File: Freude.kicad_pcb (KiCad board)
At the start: 4 copper layers, 1 part, among them U1 1CA027Pinnacle

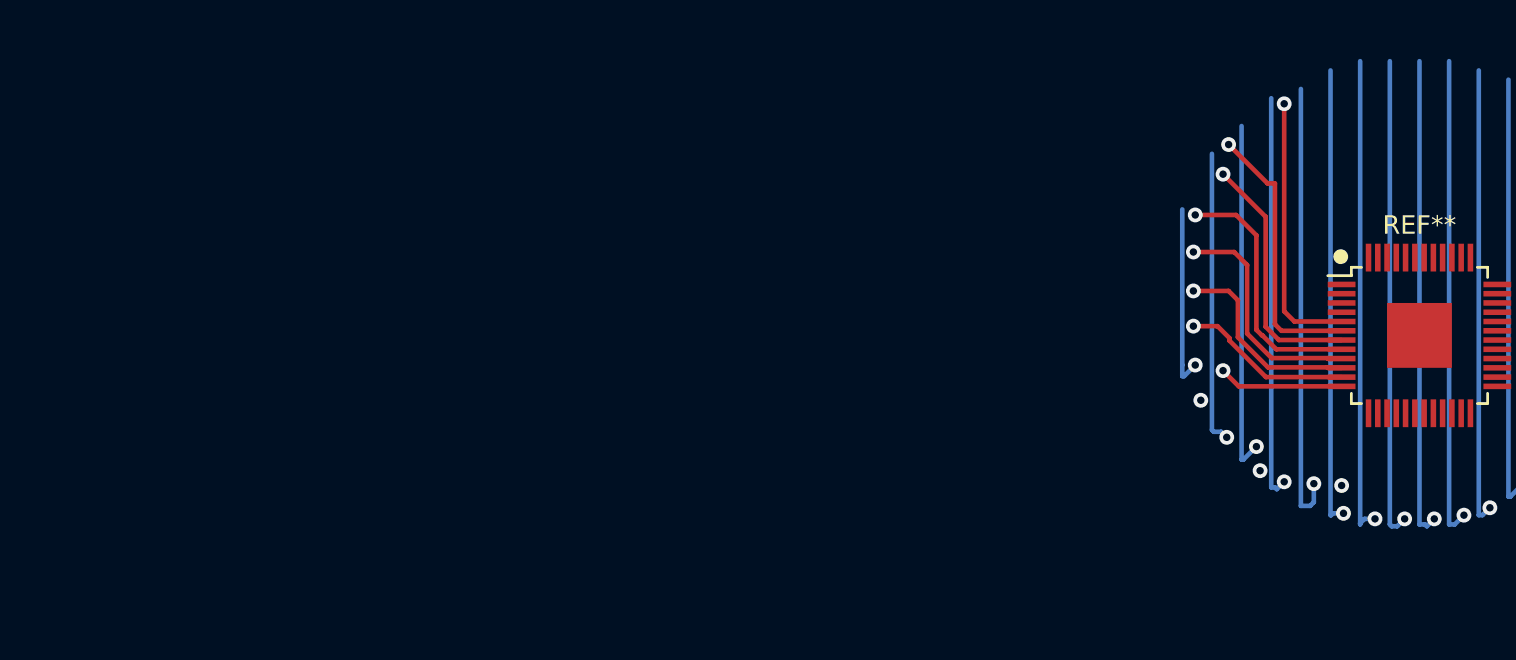
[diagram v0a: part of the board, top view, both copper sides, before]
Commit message: added a 7x8 diamond touch sensor as a sketch
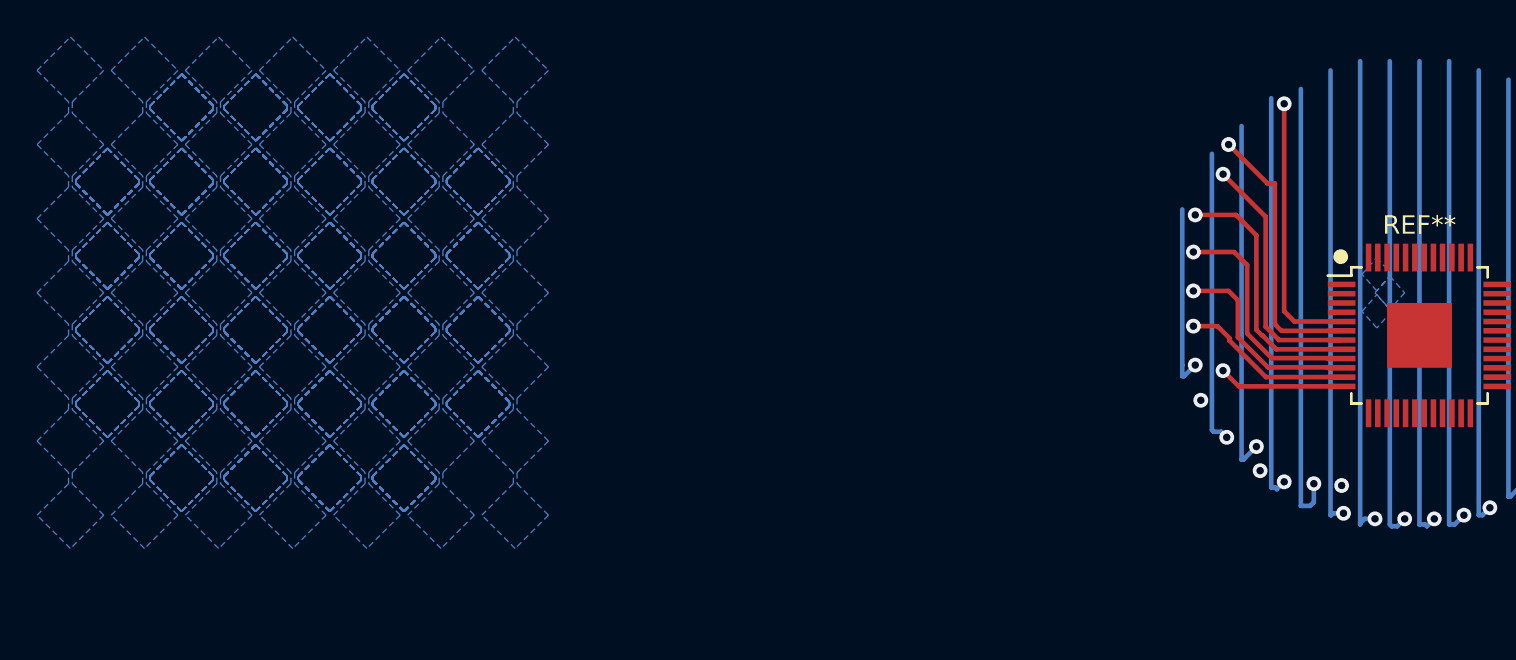
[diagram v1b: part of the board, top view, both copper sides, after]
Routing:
- added copper zone on B.Cu, net (none)
- added copper zone on B.Cu, net XA07
- added copper zone on B.Cu, net YA06
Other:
- net class Default: clearance 0.2 -> 0.018
- rule trace_clearance: 0.2 -> 0.018

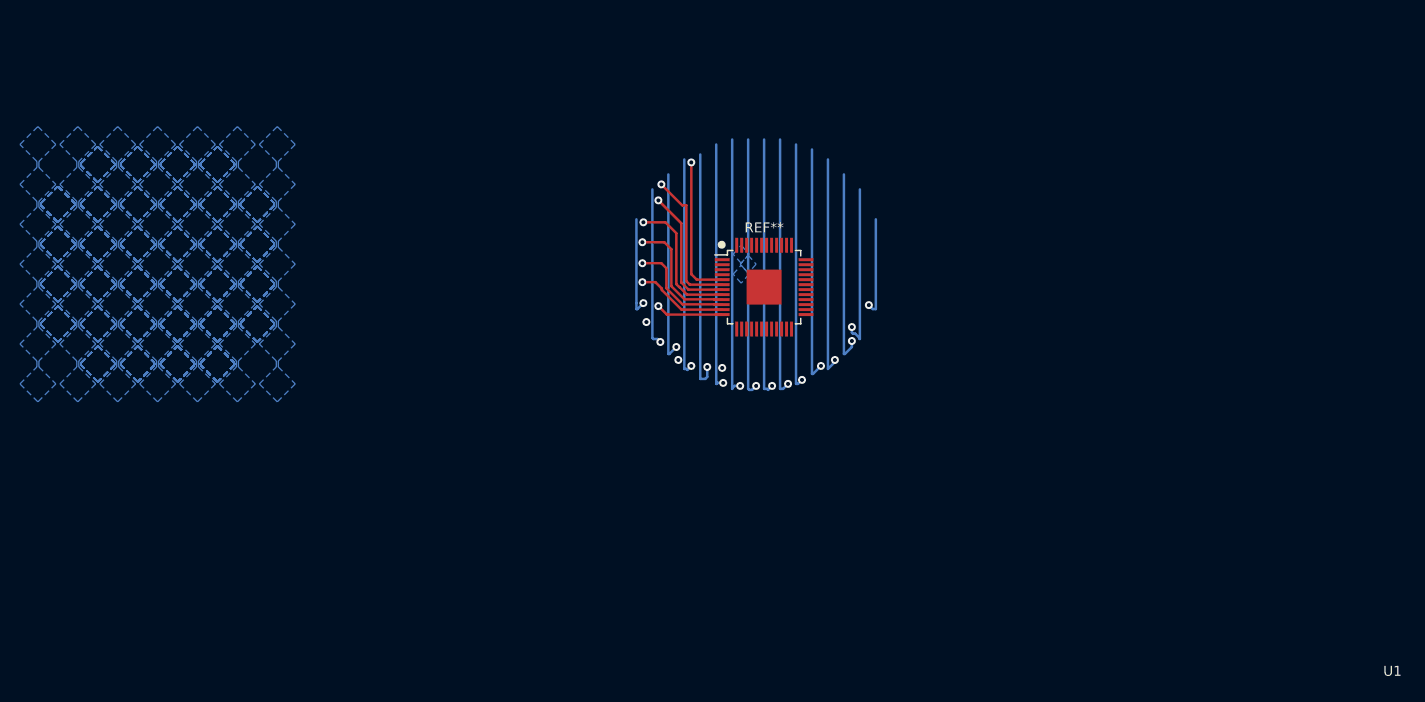
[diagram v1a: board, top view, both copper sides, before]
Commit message: azoteq IQS562 as new touch controller
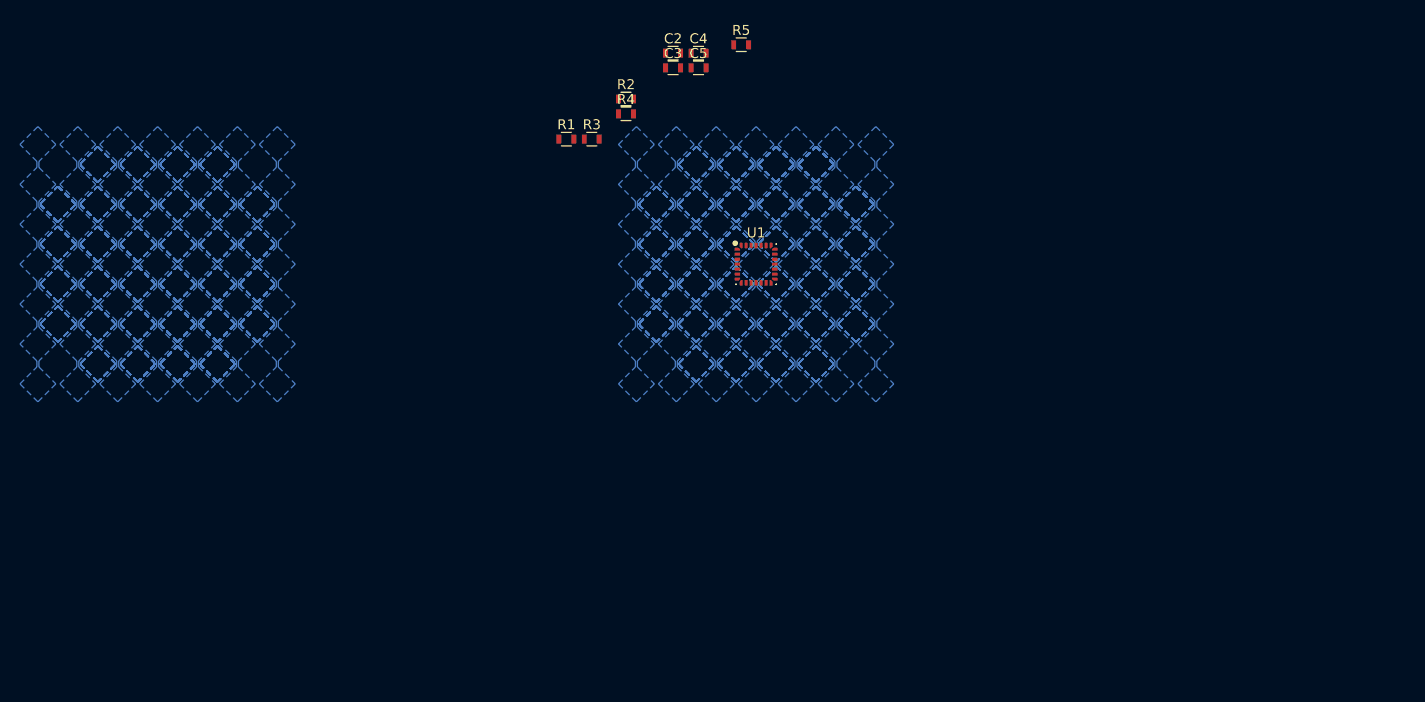
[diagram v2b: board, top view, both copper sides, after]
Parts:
- added C2: 100pF, Resistors_SMD:R_0603, F.Cu at (151.7, 58.8)
- added C3: 1uF, Resistors_SMD:R_0603, F.Cu at (151.7, 60.3)
- added C4: 100pF, Resistors_SMD:R_0603, F.Cu at (154.2, 58.8)
- added C5: 1uF, Resistors_SMD:R_0603, F.Cu at (154.2, 60.3)
- added R1: 4.7k, Resistors_SMD:R_0603, F.Cu at (141.0, 67.5)
- added R2: 4.7k, Resistors_SMD:R_0603, F.Cu at (147.0, 63.4)
- added R3: 0, Resistors_SMD:R_0603, F.Cu at (143.5, 67.5)
- added R4: 0, Resistors_SMD:R_0603, F.Cu at (147.0, 64.9)
- added R5: 0, Resistors_SMD:R_0603, F.Cu at (158.5, 58.0)
- U1: value 1CA027Pinnacle -> IQS572; footprint 1CA027Pinnacle:1CA027Pinnacle-TQFP48 -> IQS572_Library:IQS572
- moved U1 2.44 mm to (160.0, 80.0)
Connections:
- net XA10 renamed /PGM
- net XA11 renamed /SW_IN
- U1 pad 10: YA05 -> YA00
- U1 pad 11: YA06 -> YA01
- U1 pad 12: YA07 -> YA02
- U1 pad 13: YA08 -> YA03
- U1 pad 14: YA09 -> YA04
- U1 pad 15: YA10 -> YA05
- U1 pad 16: YA11 -> Net-(R5-Pad1)
- U1 pad 17: XA00 -> Net-(R4-Pad1)
- U1 pad 18: XA01 -> XA00
- U1 pad 19: XA02 -> XA01
- U1 pad 2: Net-(U1-Pad2) -> /SDA
- U1 pad 20: XA03 -> XA02
- U1 pad 21: XA04 -> XA03
- U1 pad 22: XA05 -> XA04
- U1 pad 23: XA06 -> XA05
- U1 pad 24: XA07 -> XA06
- U1 pad 25: XA08 -> XA07
- U1 pad 26: XA09 -> Net-(R3-Pad1)
- U1 pad 3: Net-(U1-Pad3) -> /SCL
- U1 pad 4: Net-(U1-Pad4) -> +3V3
- U1 pad 5: YA00 -> GND
- U1 pad 6: YA01 -> Net-(C2-Pad2)
- U1 pad 7: YA02 -> (no net)
- U1 pad 8: YA03 -> /RDY
- U1 pad 9: YA04 -> Net-(U1-Pad9)
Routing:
- net YA03: track 36.9 -> 0.00 mm, vias 1 -> 0
- net YA04: track 36.5 -> 0.00 mm, vias 1 -> 0
- net YA05: track 35.9 -> 0.00 mm, vias 1 -> 0
- net YA02: track 34.6 -> 0.00 mm, vias 1 -> 0
- net YA06: track 34.2 -> 0.00 mm, vias 1 -> 0
- net YA01: track 32.7 -> 0.00 mm, vias 1 -> 0
- net YA07: track 30.8 -> 0.00 mm, vias 1 -> 0
- net YA00: track 27.5 -> 0.00 mm, vias 1 -> 0
- net XA07: track 26.0 -> 0.00 mm, vias 1 -> 0
- net XA09: track 26.0 -> 0.00 mm, vias 1 -> 0
- net XA08: track 26.0 -> 0.00 mm, vias 1 -> 0
- net XA06: track 26.0 -> 0.00 mm, vias 1 -> 0
- net /PGM: track 24.8 -> 0.00 mm, vias 1 -> 0
- net XA05: track 24.7 -> 0.00 mm, vias 1 -> 0
- net XA04: track 24.3 -> 0.00 mm, vias 1 -> 0
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- removed copper zone on B.Cu, net YA06
